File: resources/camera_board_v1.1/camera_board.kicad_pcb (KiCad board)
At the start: 2 copper layers, 10 parts, among them P1 CONN_01X02

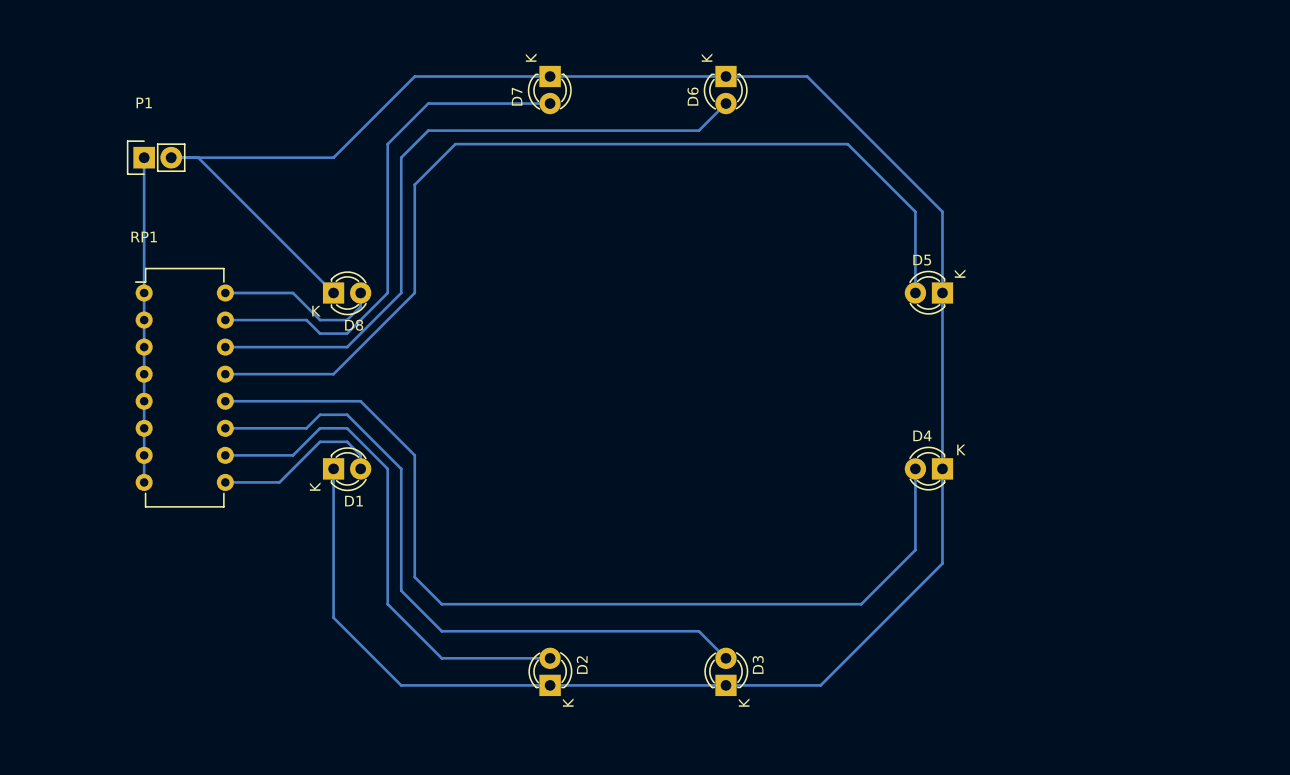
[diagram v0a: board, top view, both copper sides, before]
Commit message: changed pcb layout, changed installation instructions
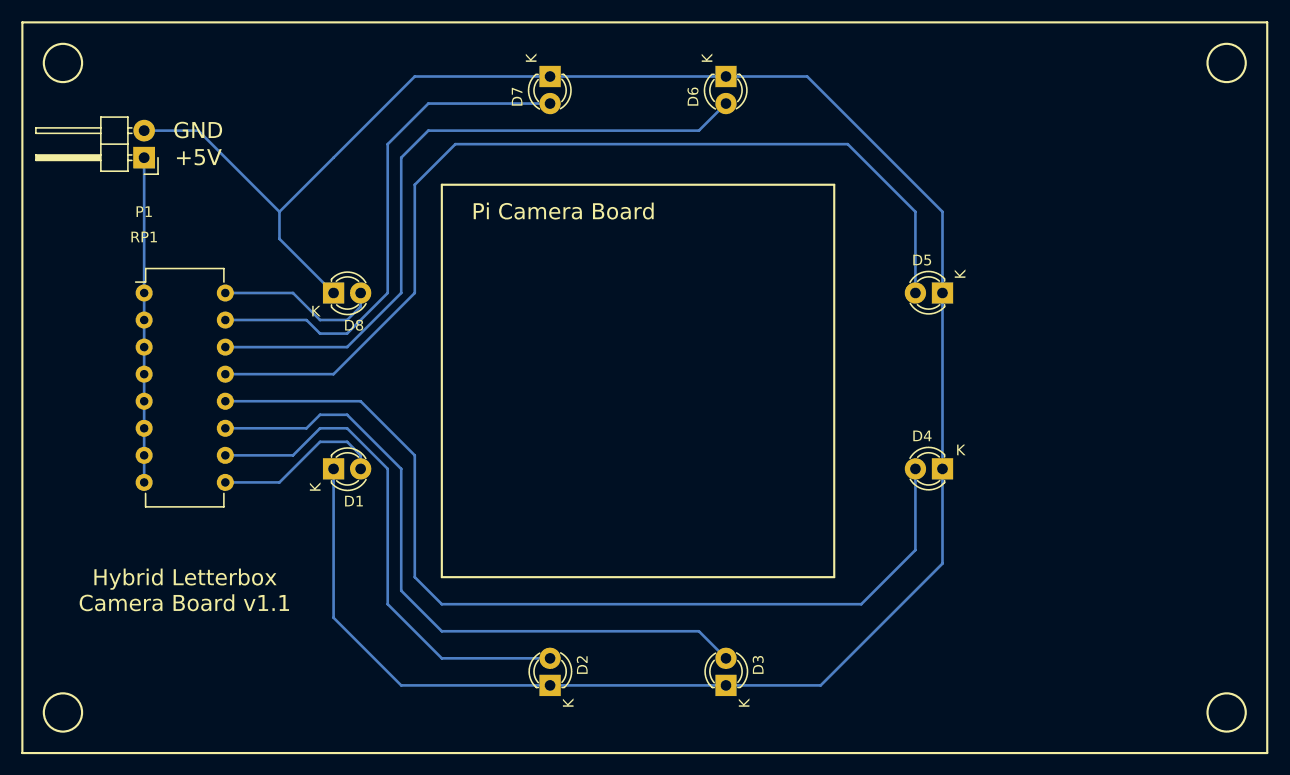
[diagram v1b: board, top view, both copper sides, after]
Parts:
- P1: footprint Socket_Strips:Socket_Strip_Straight_1x02 -> Pin_Headers:Pin_Header_Angled_1x02
- turned P1 to 180 degrees
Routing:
- net GND: track 212.8 -> 209.8 mm
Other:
- board text added: "+5V"
- board text added: "GND"
